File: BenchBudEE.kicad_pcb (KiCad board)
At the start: 4 copper layers, 165.1 x 63.5 mm, 123 parts, among them K1 1461069-5, P1 24 pin MiniFit JR, P2 CONN_2, P3 CONN_3X2, P4 12 Pin Terminal Block, P5 3 Pin TB, Q1 1461069-5, Q2 DMN65D8L-7, Q3 AOD476, Q4 AOD476, SW1 Power Switch, U1 6N137S-TA1, U10 MCP3901, U11 LMT84, U2 AP5726, U3 MCP4801, U4 OPA4170, U5 LM317K, U6 LM337T, U7 LM337T, U8 LM317

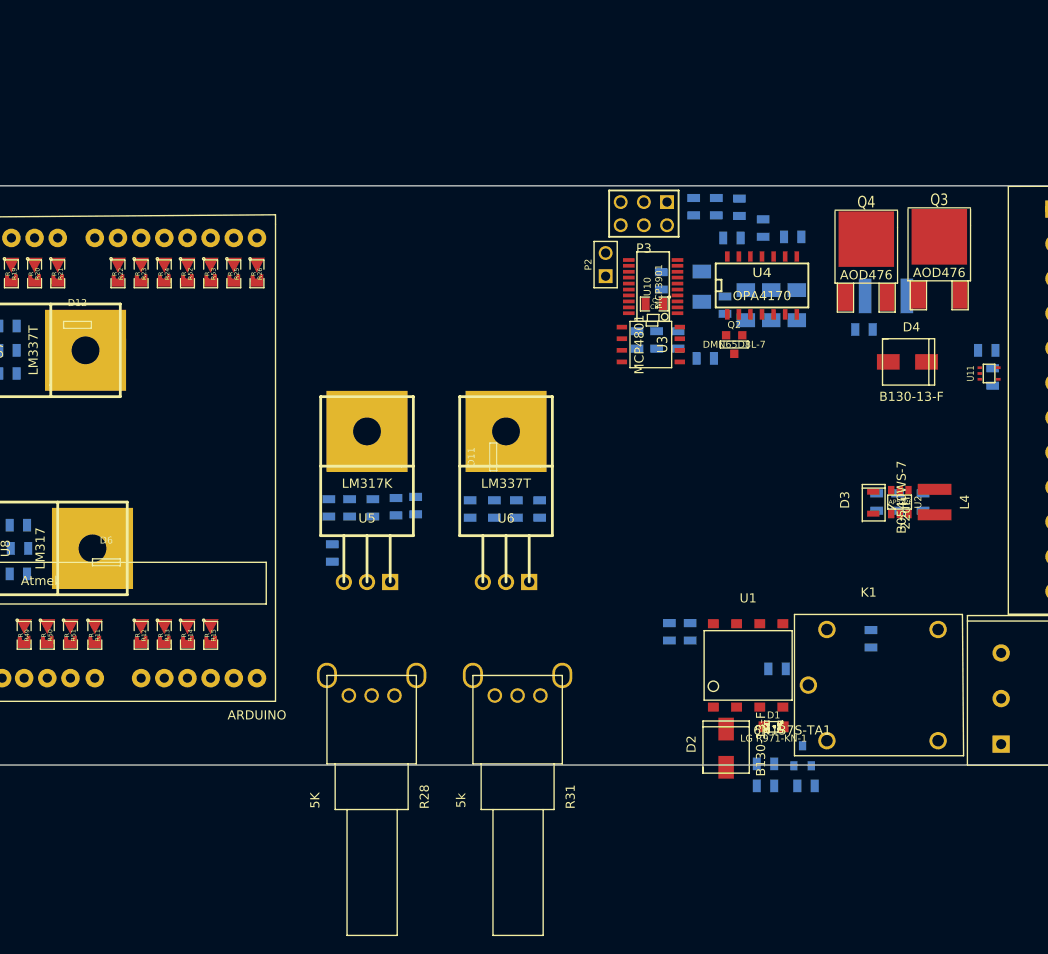
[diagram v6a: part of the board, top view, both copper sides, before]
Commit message: 5.13 Video 2/2 Finalizing The System Part Placement
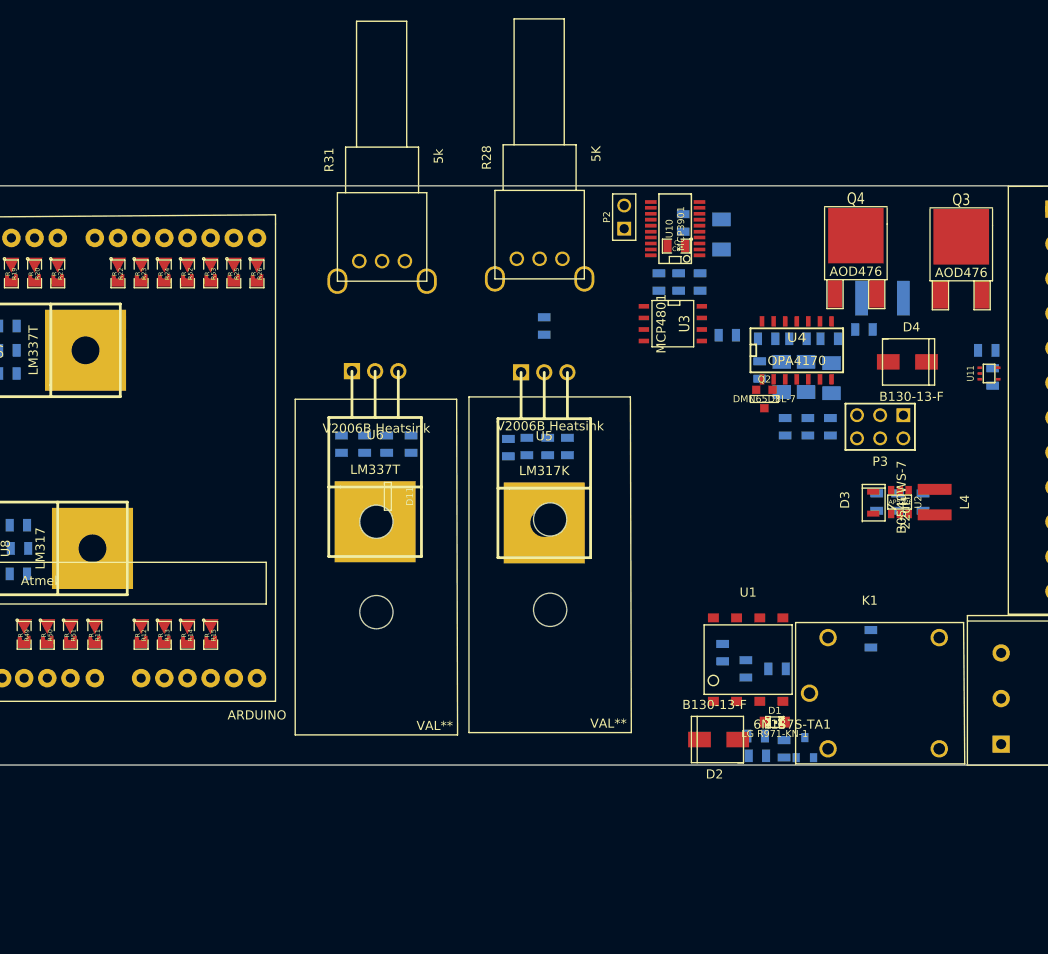
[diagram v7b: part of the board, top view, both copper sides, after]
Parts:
- added V2006B Heatsink: VAL**, V2006B_Heatsink, F.Cu at (211.3, 157.1)
- added V2006B Heatsink: VAL**, V2006B_Heatsink, F.Cu at (230.4, 156.8)
- D12, D6: moved to B.Cu
- moved R28 51.3 mm to (238.1, 104.9), turned to 90 degrees
- moved R31 49.9 mm to (220.9, 105.2), turned to 90 degrees
- moved P3 34.9 mm to (275.5, 123.3)
- moved C25 34.9 mm to (191.4, 111.9), turned to 0 degrees
- moved U5 30.1 mm to (238.6, 117.3), turned to 270 degrees
- moved U6 27.2 mm to (220.1, 117.2), turned to 270 degrees
- moved R45 26.1 mm to (267.5, 123.3)
- moved R44 26.1 mm to (265.0, 123.3)
- moved R46 26.0 mm to (270.0, 123.3)
- moved C17 24.8 mm to (241.2, 125.5), turned to 270 degrees
- moved R29 24.2 mm to (238.6, 112.3), turned to 270 degrees
- moved R30 22.9 mm to (216.4, 125.2), turned to 270 degrees
- moved D9 22.1 mm to (238.3, 134.7), turned to 270 degrees
- moved R34 20.8 mm to (234.7, 125.6), turned to 270 degrees
- moved D5 20.6 mm to (238.5, 132.6), turned to 270 degrees
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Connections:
- C24 pad 2: (no net) -> FE_V-
- C25 pad 1: (no net) -> FE_V-
- C25 pad 2: (no net) -> /PowerAdjustmentMonitor/V-_ADJ

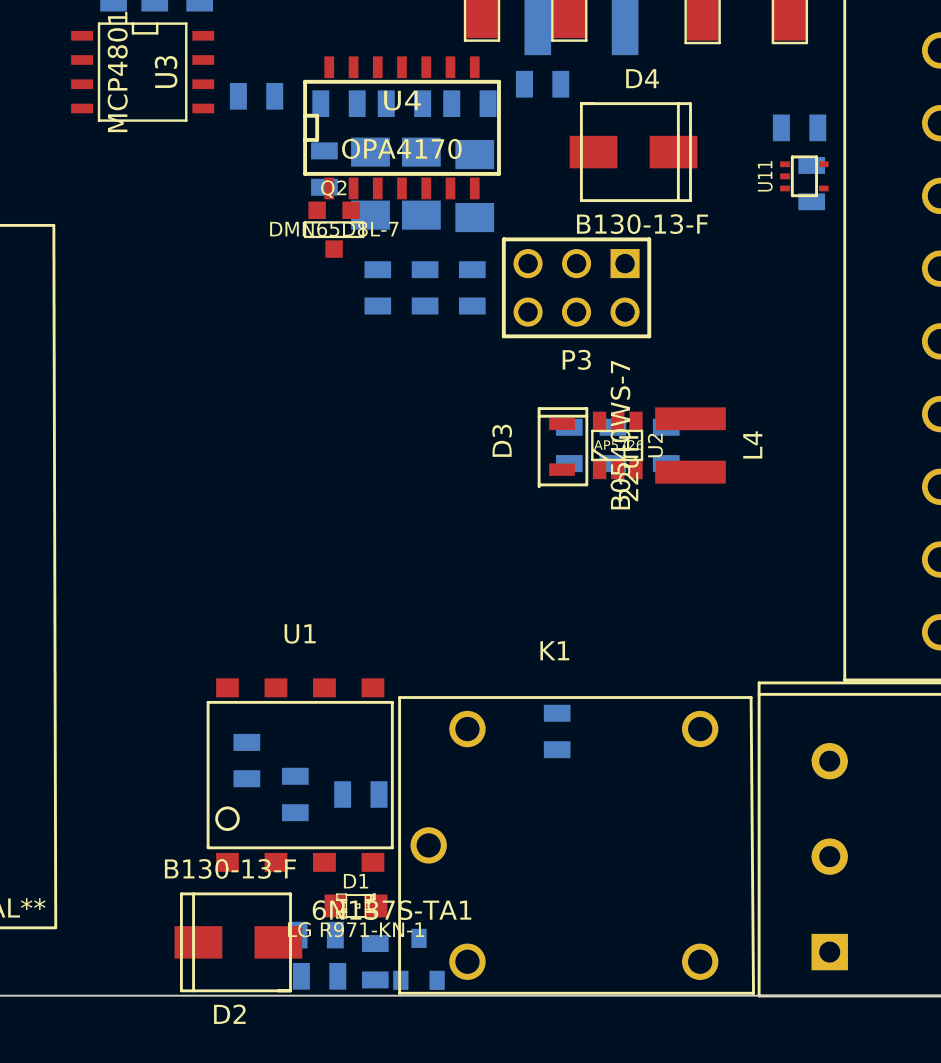
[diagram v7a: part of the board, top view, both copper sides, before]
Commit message: Cleanup/ERC checks, etc (on my own, no video)
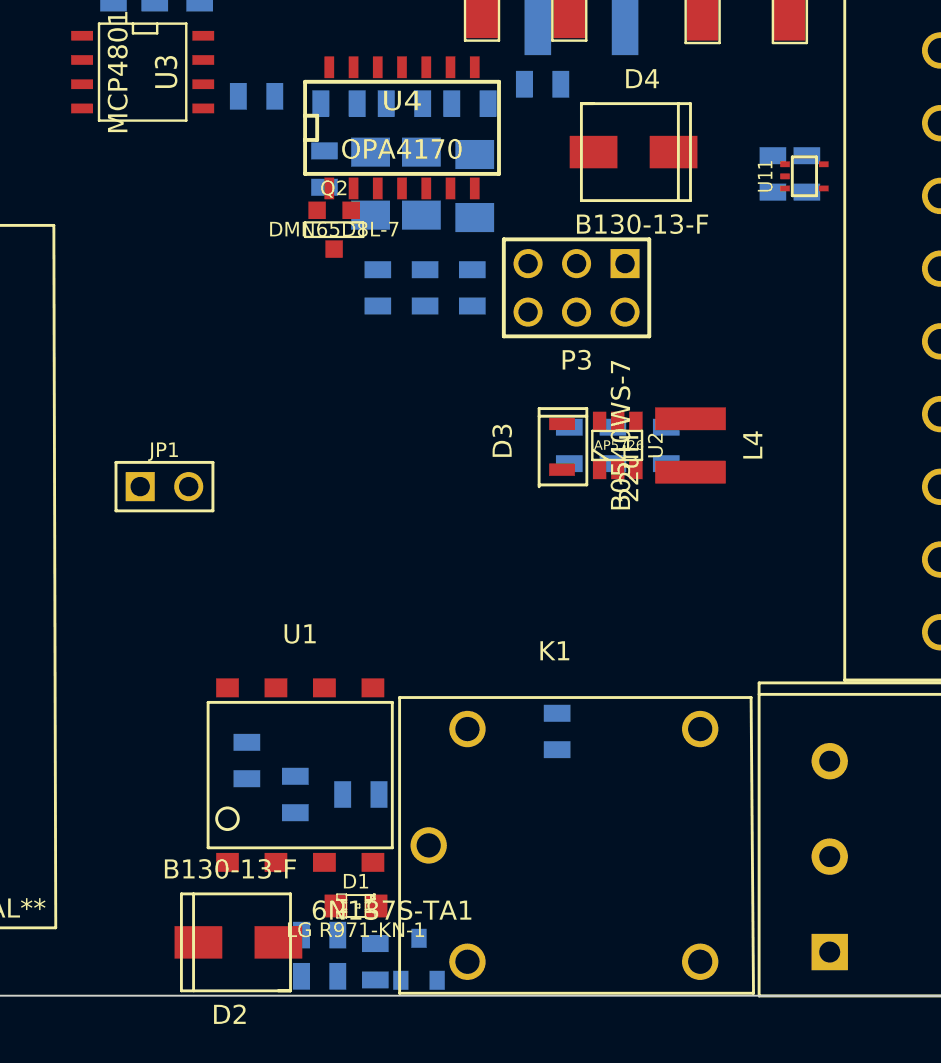
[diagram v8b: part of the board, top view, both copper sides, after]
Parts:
- added JP1: JUMPER, PIN_ARRAY_2X1, F.Cu at (253.9, 133.7)
- moved R48 2.79 mm to (285.8, 117.3), turned to 270 degrees
- moved C7 0.57 mm to (287.5, 117.3)
- moved R2 0.13 mm to (262.0, 157.2)
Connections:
- C21 pad 2: (no net) -> N-00000136
- D7 pad 1: N-00000137 (its old number) -> N-00000136
- R32 pad 2: N-00000137 (its old number) -> N-00000136
- R33 pad 1: N-00000137 (its old number) -> N-00000136
- R8 pad 1: (no net) -> /LED_Driver/LED_STRING-
- U7 pad 1: N-00000137 (its old number) -> N-00000136
